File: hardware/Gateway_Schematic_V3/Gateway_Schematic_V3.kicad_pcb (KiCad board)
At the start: 2 copper layers, 193.2 x 111.3 mm, 218 parts, among them IC1 RTC_DS3231M, IC2 SIM7600CE-H, J1 USB_C_Receptacle_USB2.0_14P, J10 ANT_LTE, J11 ANT_LTE, J12 ANT_LTE, J14 SIM7100-6pin-socket-smd, J17 HR911105A, J2 Conn_01x04_Pin, J3 Screw_Terminal_01x03, J5 MiSD-PP-9P-V1, J6 Conn_01x07_Pin, Q1 MMBT3904, Q2 BC817, Q3 BC817, Q4 BC817, Q8 MMBT3904, SW1 SW_Push, SW2 SW_Push, U1 ESP32-S3-WROOM-1, U11 TPS5430DDA, U4 AMS1117-3.3, U7 TPS5430DDA, U8 SX1278 Lora Ra-02, U9 W5500, Y2 25MHz

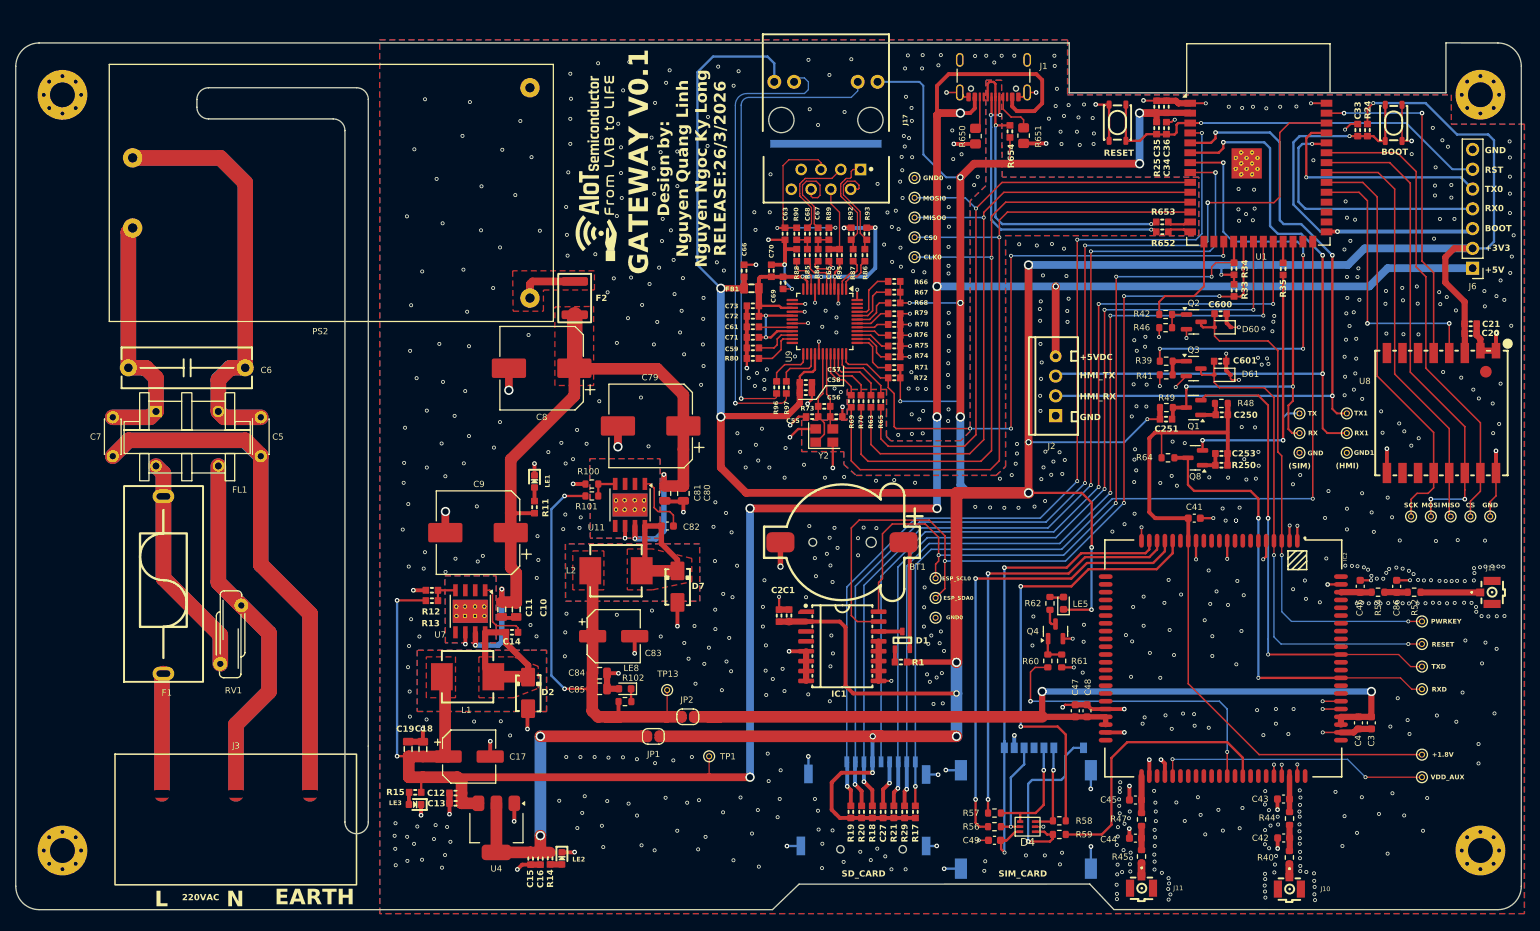
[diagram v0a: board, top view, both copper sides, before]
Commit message: Update Capacital for Shield of Ethernet
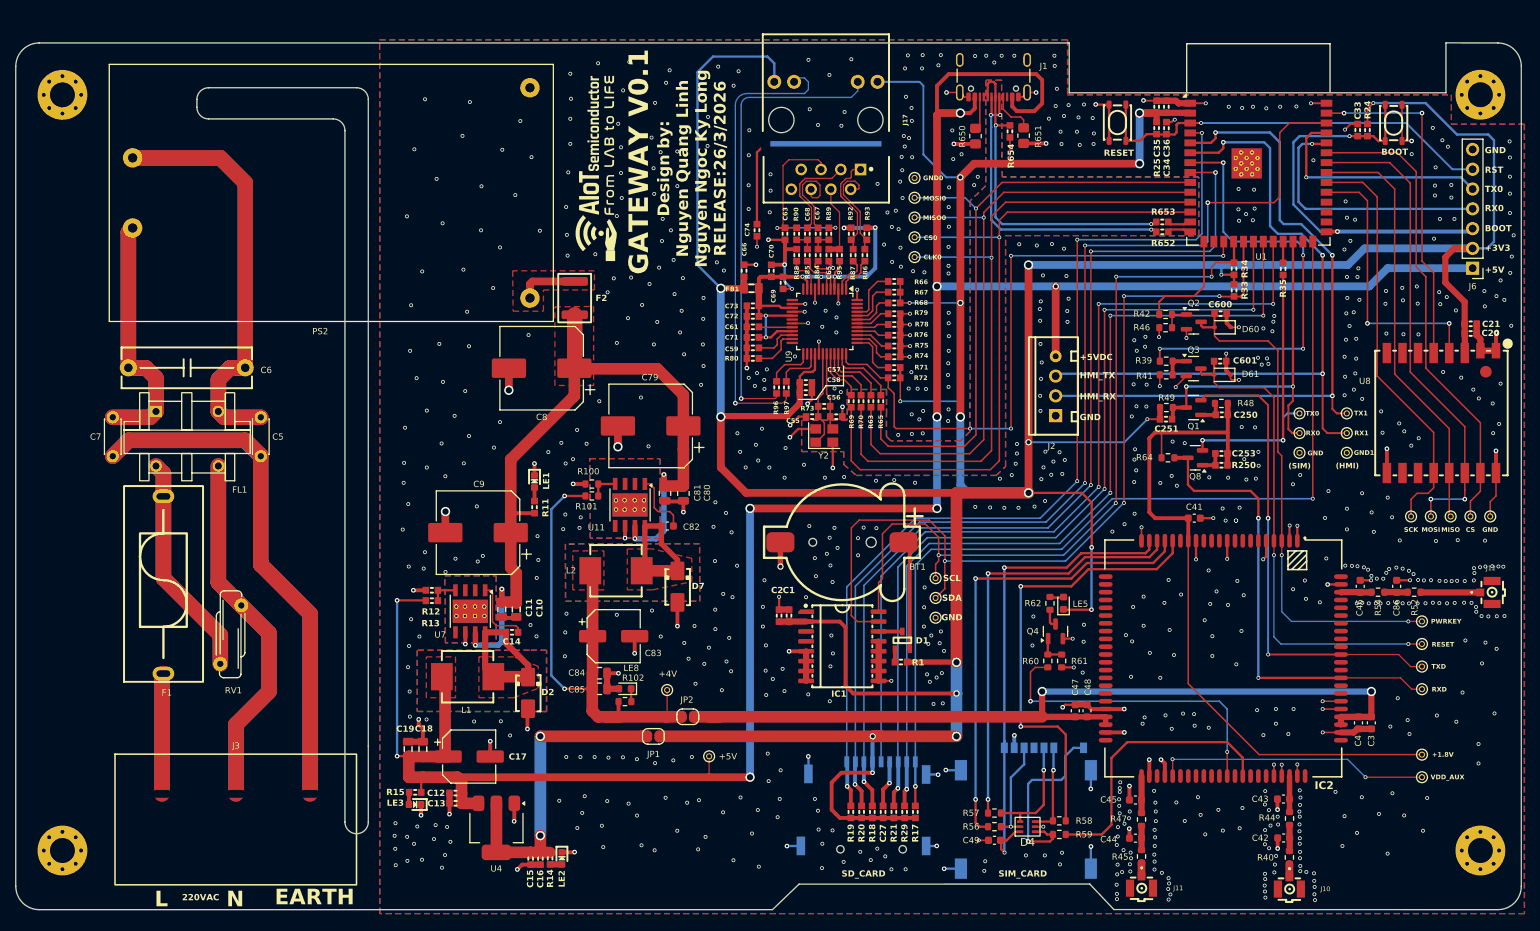
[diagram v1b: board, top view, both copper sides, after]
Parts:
- added C74: 10nF, IVS_FOOTPRINTS:C_0603, F.Cu at (225.4, 165.5)
- renumbered TP13 to +4V, TP1 to +5V, GND0 to GND, RX to RX0, ESP_SCL0 to SCL, ESP_SDA0 to SDA, TX to TX0
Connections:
- J17 pad SH: unconnected-(J17-SHIELD-PadSH) -> Net-(J17-SHIELD)
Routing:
- net Net-(J17-SHIELD): track 0.00 -> 26.3 mm
- net unconnected-(J17-SHIELD-PadSH): track 15.5 -> 0.00 mm
- net GND: track 285.6 -> 288.4 mm, vias 891 -> 896

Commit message: Update PCB Layout after review 27/3/2026
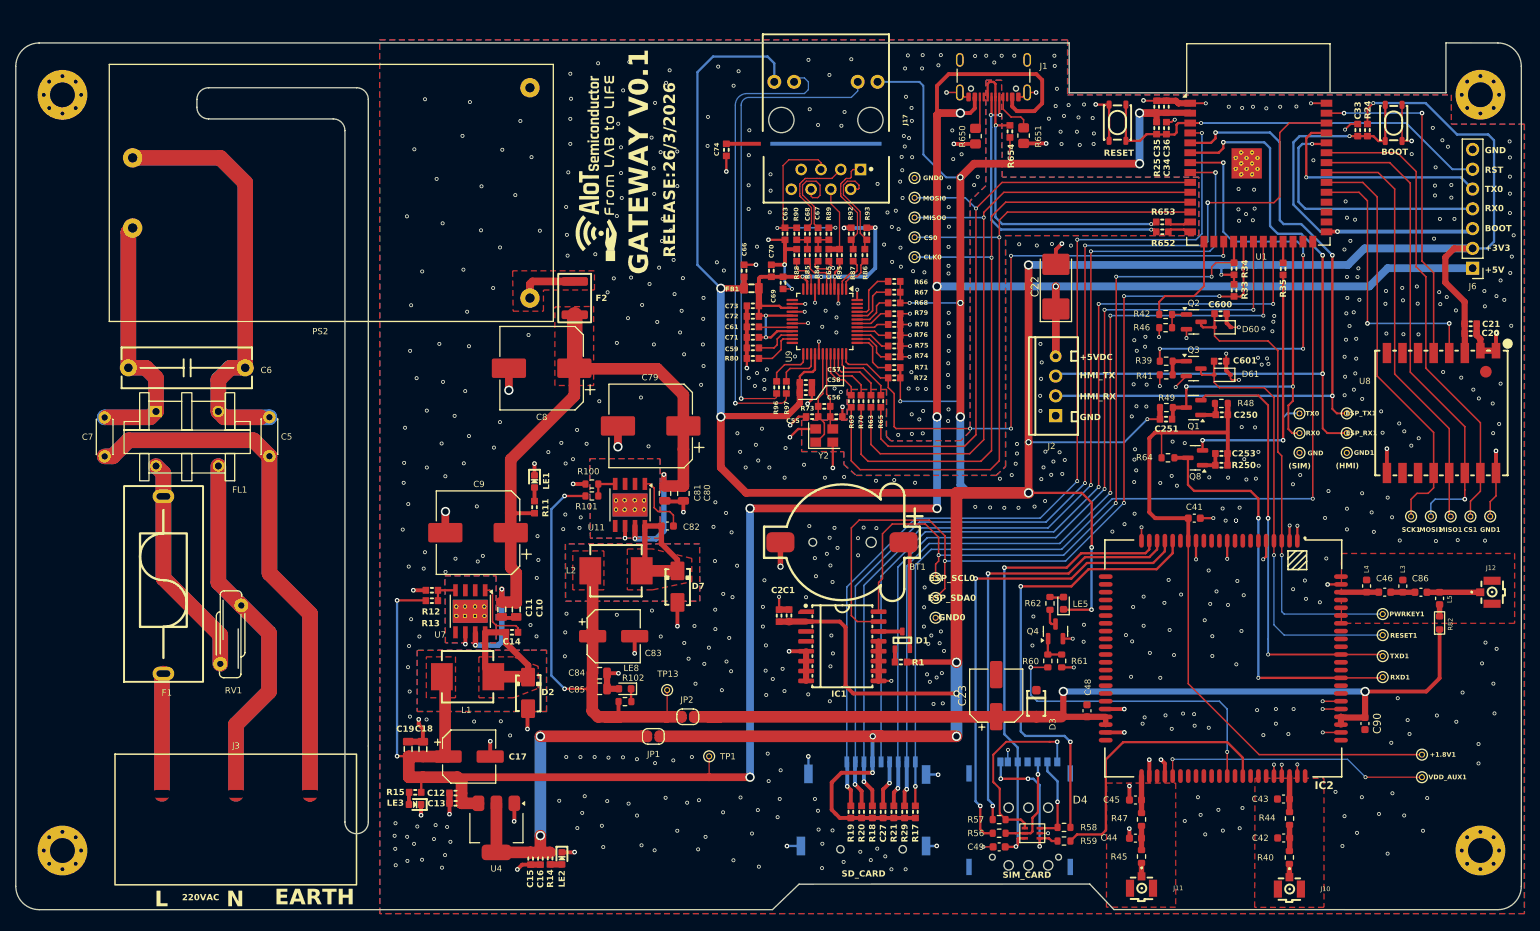
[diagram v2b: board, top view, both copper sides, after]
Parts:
- removed C3, C47: 100nF, Capacitor_SMD:C_0603_1608Metric
- removed C4: 10uF, Capacitor_SMD:C_0603_1608Metric
- removed R52, R54: 0, Resistor_SMD:R_0603_1608Metric
- added C22: 100uF/35V/7343, Capacitor_Tantalum_SMD:CP_EIA-7132-28_AVX-C_Pad2.72x3.50mm_HandSolder, F.Cu at (263.8, 172.8)
- added C23: C_Polarized, IVS_NEW_FOOTPRINT:CP_Elec_6.3x7.7, F.Cu at (256.1, 225.3)
- added C90: 18pF, Capacitor_SMD:C_0603_1608Metric, F.Cu at (303.4, 228.9)
- added D3: 5V1, IVS_NEW_FOOTPRINT:D_SOD-123, F.Cu at (261.2, 226.2)
- added L3: L, IVS_NEW_FOOTPRINT:L_0603_1608Metric, F.Cu at (308.3, 211.2)
- added L4: L, IVS_NEW_FOOTPRINT:L_0603_1608Metric, F.Cu at (303.6, 211.2)
- added L5: L, IVS_NEW_FOOTPRINT:L_0603_1608Metric, F.Cu at (313.0, 212.8)
- added R82: 10 Ohm, IVS_NEW_FOOTPRINT:R_0603_1608Metric, F.Cu at (313.0, 215.9)
- C1, C20: value 1uF -> 10uF
- C46, C86: value NC -> 33pF
- C48: value 10uF -> 33pF
- C74: value 10nF -> 4.7nF
- J14: footprint GATEWAY_LIB:GCT_SIM7100-6-socket-smd -> IVS_NEW_FOOTPRINT:CUI_NSIM-1-A
- moved C74 11.0 mm to (221.5, 155.2)
- moved J14 7.56 mm to (259.1, 248.0)
- moved RXD1 5.27 mm to (305.7, 222.9)
- moved TXD1 5.22 mm to (305.7, 220.2)
- moved RESET1 5.17 mm to (305.7, 217.5)
- moved PWRKEY1 5.13 mm to (305.7, 214.8)
- moved C46 3.23 mm to (306.0, 212.0), turned to 0 degrees
- moved C86 3.21 mm to (310.6, 212.0), turned to 0 degrees
- moved C5 1.11 mm to (162.8, 189.5)
- moved C7 1.04 mm to (141.7, 194.6)
- moved R58 1.03 mm to (264.8, 242.2)
- moved R59 1.03 mm to (264.8, 243.9)
- moved C49 1.03 mm to (256.5, 244.7)
- moved D4 1.03 mm to (260.7, 242.9)
- moved R56 1.03 mm to (256.5, 242.9)
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- renumbered +1.8V to +1.8V1, CS to CS1, RX1 to ESP_RX1, SCL to ESP_SCL0, SDA to ESP_SDA0, TX1 to ESP_TX1, GND to GND0, GND to GND1, MISO to MISO1, MOSI to MOSI1, PWRKEY to PWRKEY1, RESET to RESET1, RXD to RXD1, SCK to SCK1, +5V to TP1, +4V to TP13, TXD to TXD1, VDD_AUX to VDD_AUX1
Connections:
- C1 pad 2: +3V3 -> +3.3V
- C2 pad 2: +3V3 -> +3.3V
- C20 pad 1: +3V3 -> +3.3V
- C21 pad 1: +3V3 -> +3.3V
- C251 pad 1: +3V3 -> +3.3V
- C27 pad 2: +3V3 -> +3.3V
- C35 pad 1: +3V3 -> +3.3V
- C36 pad 1: +3V3 -> +3.3V
- C46 pad 1: GND -> Net-(IC2-GNSS_ANT)
- C46 pad 2: Net-(IC2-GNSS_ANT) -> Net-(C46-Pad2)
- C57 pad 1: +3V3 -> +3.3V
- C58 pad 1: +3V3 -> +3.3V
- C66 pad 1: +3V3 -> +3.3V
- C83 pad 1: /Khối nguồn/4v_SIM -> +4V
- C84 pad 1: /Khối nguồn/4v_SIM -> +4V
- C85 pad 1: /Khối nguồn/4v_SIM -> +4V
- C86 pad 1: GND -> Net-(C46-Pad2)
- C86 pad 2: Net-(C86-Pad2) -> Net-(J12-In)
- FB1 pad 2: +3V3 -> +3.3V
- IC1 pad 2: +3V3 -> +3.3V
- J17 pad 12: +3V3 -> +3.3V
- J17 pad 9: +3V3 -> +3.3V
- J5 pad 4: +3V3 -> +3.3V
- J6 pad 2: +3V3 -> +3.3V
- JP1 pad 2: +3V3 -> +3.3V
- JP2 pad 1: /Khối nguồn/4v_SIM -> +4V
- L2 pad 2: /Khối nguồn/4v_SIM -> +4V
- LE5 pad 1: +3V3 -> +3.3V
- R1 pad 1: +3V3 -> +3.3V
- R101 pad 2: /Khối nguồn/4v_SIM -> +4V
- R102 pad 1: /Khối nguồn/4v_SIM -> +4V
- R14 pad 1: +3V3 -> +3.3V
- R17 pad 1: +3V3 -> +3.3V
- R18 pad 1: +3V3 -> +3.3V
- R19 pad 1: +3V3 -> +3.3V
- R20 pad 1: +3V3 -> +3.3V
- R21 pad 1: +3V3 -> +3.3V
- R24 pad 1: +3V3 -> +3.3V
- R25 pad 1: +3V3 -> +3.3V
- R29 pad 1: +3V3 -> +3.3V
- R33 pad 1: +3V3 -> +3.3V
- R34 pad 1: +3V3 -> +3.3V
- R49 pad 2: +3V3 -> +3.3V
- R654 pad 2: +3V3 -> +3.3V
- R66 pad 1: +3V3 -> +3.3V
- R67 pad 1: +3V3 -> +3.3V
- R68 pad 1: +3V3 -> +3.3V
- R71 pad 1: +3V3 -> +3.3V
- R72 pad 1: +3V3 -> +3.3V
- TP13 pad 1: /Khối nguồn/4v_SIM -> +4V
- U1 pad 2: +3V3 -> +3.3V
- U8 pad 3: +3V3 -> +3.3V
- U9 pad 28: +3V3 -> +3.3V
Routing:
- net +3.3V: track 41.6 -> 632.5 mm, vias 2 -> 24
- net +3V3: track 590.9 -> 0.00 mm, vias 22 -> 0
- net +4V: track 108.7 -> 192.2 mm, vias 2 -> 4
- net /Khối nguồn/4v_SIM: track 70.7 -> 0.00 mm, vias 2 -> 0
- net GND: track 288.4 -> 266.8 mm, vias 896 -> 745
- net Net-(J14-CLK): track 14.5 -> 23.8 mm
- net /SIMCOM/RESET: track 63.7 -> 57.3 mm, vias 2 -> 1
- net Net-(J17-SHIELD): track 26.3 -> 20.5 mm
- net /SIMCOM/RXD: track 59.6 -> 54.0 mm
- net /SIMCOM/TXD: track 61.8 -> 56.2 mm
- net /SIMCOM/PWRKEY: track 66.3 -> 60.9 mm, vias 2 -> 1
- net Net-(D4-Pad1): track 24.2 -> 18.9 mm, vias 1 -> 3
- net Earth: track 133.4 -> 136.9 mm
- net Net-(C46-Pad2): track 0.00 -> 3.10 mm
- net Net-(C86-Pad2): track 3.01 -> 0.00 mm
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- added copper zone on F.Cu, net +4V
- removed copper zone on F.Cu, net /Khối nguồn/4v_SIM
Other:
- board text added: "Design by: Nguyen Quang Linh 22151246 Nguyen Ngoc Ky Long 22151250"
- board text added: "RELEASE:26/3/2026"
- board text removed: "Design by: Nguyen Quang Linh Nguyen Ngoc Ky Long RELEASE:26/3/2026"

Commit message: Update: add L_ferrite for SIMCOM
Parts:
- added L6: L_Ferrite_Small, IVS_NEW_FOOTPRINT:L_0805, F.Cu at (249.8, 228.0)
- renumbered TP13 to +4V, TP1 to +5V, CS1 to CS, GND1 to GND, MISO1 to MISO, MOSI1 to MOSI, ESP_RX1 to RX1, SCK1 to SCK, ESP_TX1 to TX1
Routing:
- net +4V: track 192.2 -> 196.5 mm
- net GND: track 266.8 -> 267.3 mm, vias 745 -> 928

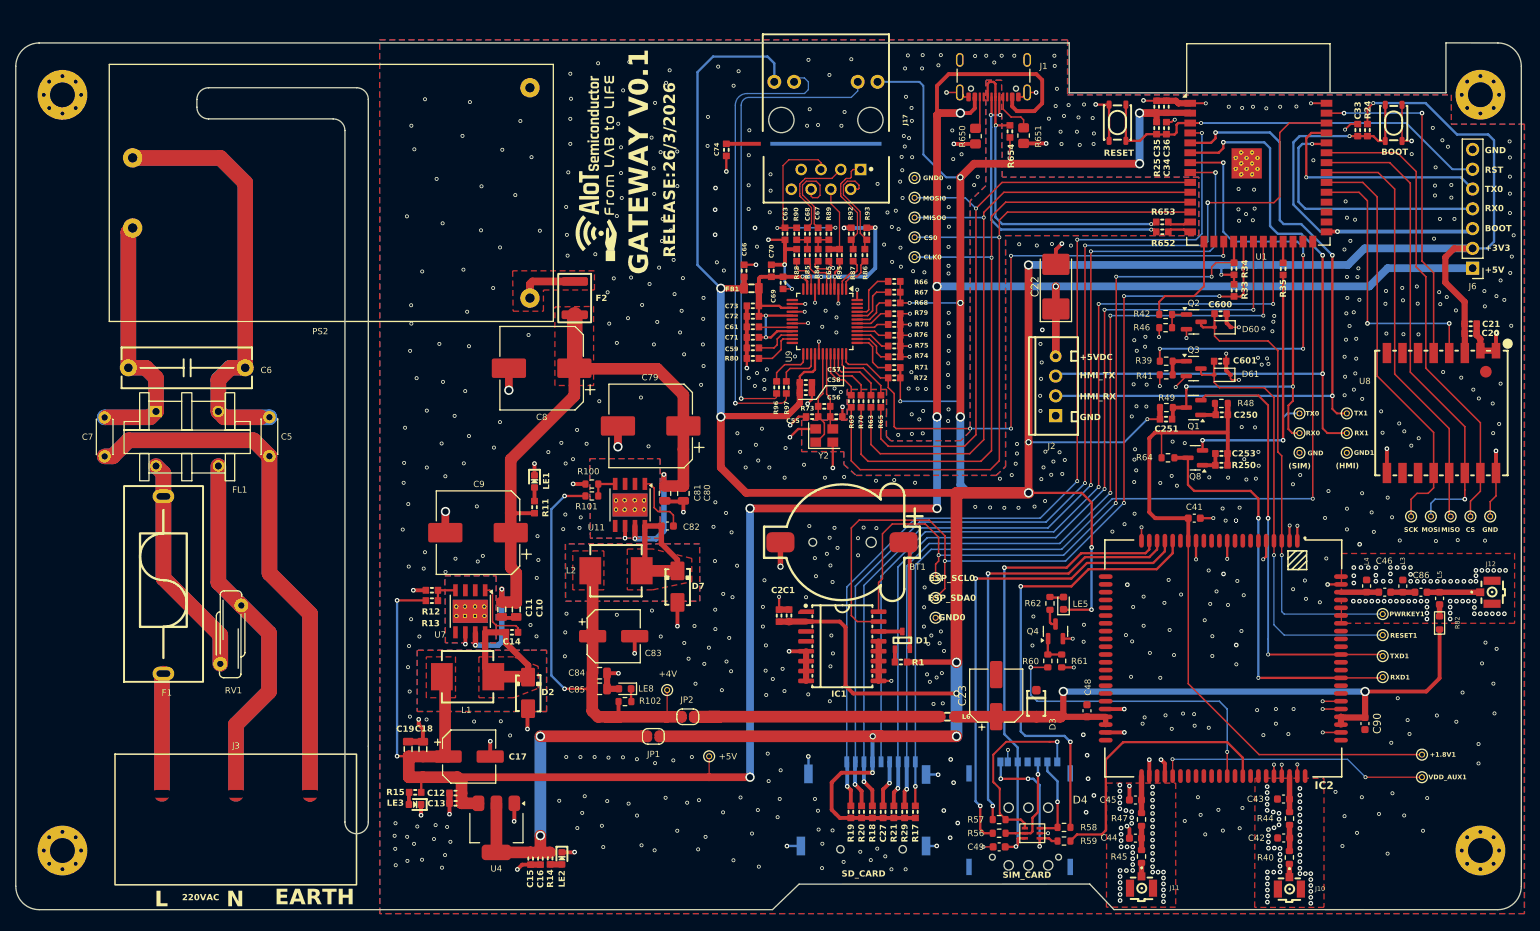
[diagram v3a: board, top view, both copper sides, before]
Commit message: Update PCB_Layout for Gateway (31/3/2026)
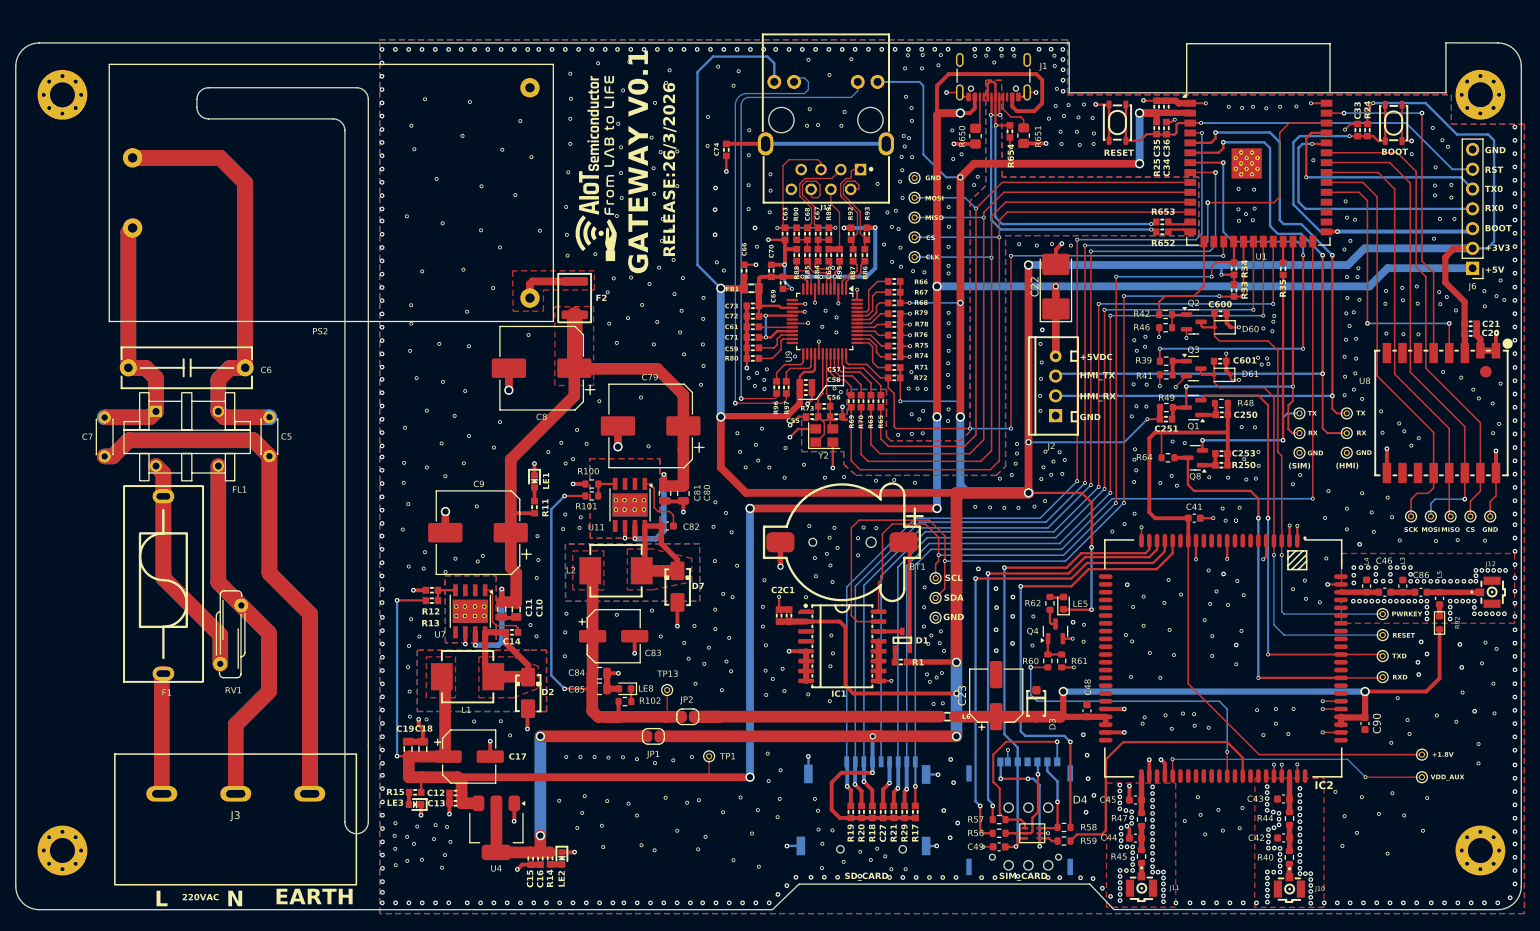
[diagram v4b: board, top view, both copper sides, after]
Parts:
- renumbered +1.8V1 to +1.8V, CLK0 to CLK, CS0 to CS, GND0 to GND, GND1 to GND, MISO0 to MISO, MOSI0 to MOSI, PWRKEY1 to PWRKEY, RESET1 to RESET, RX0 to RX, RX1 to RX, RXD1 to RXD, ESP_SCL0 to SCL, ESP_SDA0 to SDA, +5V to TP1, +4V to TP13, TX0 to TX, TX1 to TX, TXD1 to TXD, VDD_AUX1 to VDD_AUX
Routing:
- net GND: vias 928 -> 1186
